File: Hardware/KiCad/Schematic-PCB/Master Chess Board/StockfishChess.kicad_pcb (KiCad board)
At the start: 4 copper layers, 100 x 120 mm, 72 parts, among them J1 ZF1-15-02-X-WT-X, J2 USB4110GFA, J4 ZF1-15-02-X-WT-X, U1 ESP32-S3-WROOM-2, U143 SN74AHCT125D, U144 USBLC6-2P6, U145 RUEF300, U146 RUEF300, U3 BQ24074RGT, U4 TPS61023DRLT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

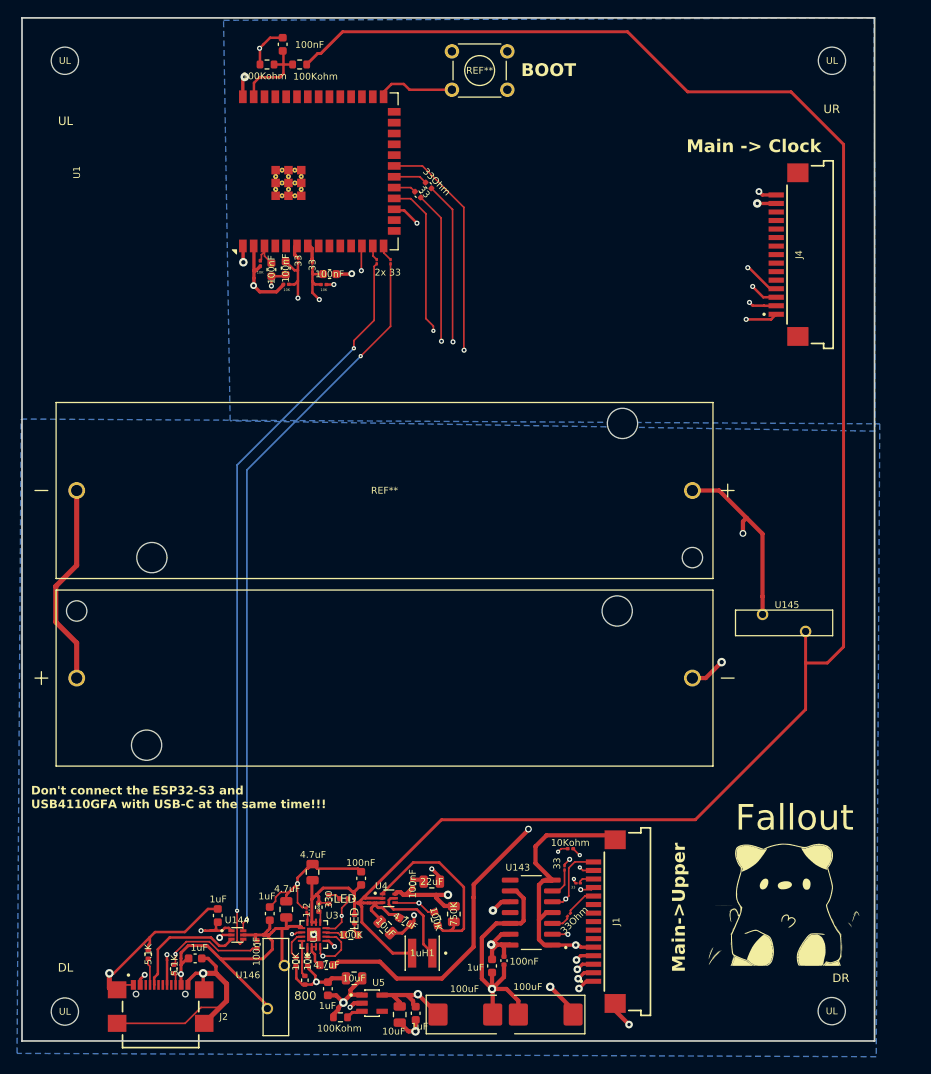
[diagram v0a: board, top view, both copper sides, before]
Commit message: Fixed some errors and finished BOM
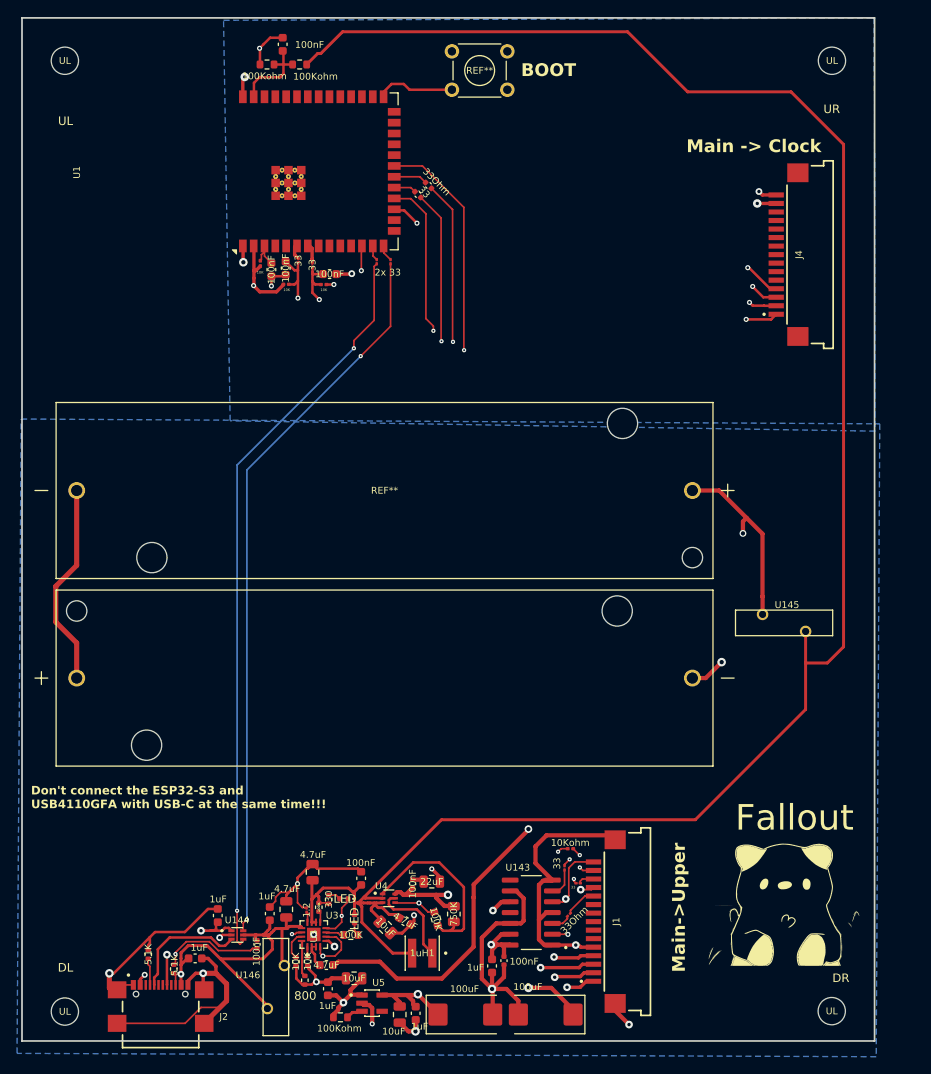
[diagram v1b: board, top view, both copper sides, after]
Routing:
- net +3.3V: track 206.1 -> 212.9 mm
- net +5V: track 41.0 -> 47.5 mm
- net GND: track 209.4 -> 211.1 mm

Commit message: Modified resistors
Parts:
- removed the 10Kohm at (139.1, 132.2)
- removed the 10Kohm at (110.1, 66.0)
- removed the 10Kohm at (105.7, 66.0)
- removed 2x 33: R_01005_0402Metric, Resistor_SMD:R_01005_0402Metric
- removed the 33Ohm at (138.4, 134.5)
- removed the 33Ohm at (108.8, 63.8)
- removed the 33Ohm at (140.0, 136.3)
- removed the 33Ohm at (138.9, 140.0)
- removed the 33Ohm at (107.1, 63.2)
- removed the REF** at (118.0, 63.4)
- added 10K: R_0402_1005Metric, Resistor_SMD:R_0402_1005Metric, F.Cu at (110.0, 66.2)
- added 10K: R_0402_1005Metric, Resistor_SMD:R_0402_1005Metric, F.Cu at (105.8, 66.3)
- added 10Kohm: R_0402_1005Metric, Resistor_SMD:R_0402_1005Metric, F.Cu at (139.0, 132.3)
- added 33: R_0402_1005Metric, Resistor_SMD:R_0402_1005Metric, F.Cu at (107.1, 63.6)
- added 33: R_0402_1005Metric, Resistor_SMD:R_0402_1005Metric, F.Cu at (118.2, 63.5)
- added 33: R_0402_1005Metric, Resistor_SMD:R_0402_1005Metric, F.Cu at (116.6, 63.6)
- added 33: R_0402_1005Metric, Resistor_SMD:R_0402_1005Metric, F.Cu at (137.8, 134.0)
- added 33: R_0402_1005Metric, Resistor_SMD:R_0402_1005Metric, F.Cu at (108.7, 63.6)
- added 33: R_0402_1005Metric, Resistor_SMD:R_0402_1005Metric, F.Cu at (139.2, 139.9)
- added 33: R_0402_1005Metric, Resistor_SMD:R_0402_1005Metric, F.Cu at (139.7, 135.8)
- 1.2: value R_01005_0402Metric -> R_0402_1005Metric; footprint Resistor_SMD:R_01005_0402Metric -> Resistor_SMD:R_0402_1005Metric
- moved 1.2 0.71 mm to (107.6, 138.9), turned to -90 degrees
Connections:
- 1.2 pad 1: Net-(U3-ILIM) -> GND
- 1.2 pad 2: GND -> Net-(U3-ILIM)
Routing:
- net GND: track 211.1 -> 209.9 mm
- net Net-(U1-IO13): track 100.4 -> 101.0 mm
- net /CLK 5V: track 10.2 -> 10.8 mm
- net Net-(J4-Pad01): track 64.6 -> 64.1 mm
- net +3.3V: track 212.9 -> 212.4 mm

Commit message: Added pulups to hall effect
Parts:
- removed the 1uF at (97.7, 140.1)
- added 100: C_0402_1005Metric, Capacitor_SMD:C_0402_1005Metric, F.Cu at (101.0, 65.1)
- added 22uF: C_1206_3216Metric, Capacitor_SMD:C_1206_3216Metric, F.Cu at (101.0, 69.1)
- added 3.3K: R_0402_1005Metric, Resistor_SMD:R_0402_1005Metric, F.Cu at (126.0, 55.2)
- added 6.8K: R_0402_1005Metric, Resistor_SMD:R_0402_1005Metric, F.Cu at (122.0, 50.5)
- turned REF** to 0 degrees
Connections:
- 4.7uF pad 1: VBUS -> BAT
- 4.7uF pad 2: VBUS -> BAT
- REF** pad N: Net-(BT1-PadN) -> GND
- REF** pad P: VBUS -> BAT
- REF** pad P: Net-(BT1-PadN) -> BAT
- U145 pad P$1: VBUS -> BAT
- U3 pad 2: VBUS -> BAT
- U3 pad 3: VBUS -> BAT
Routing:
- net BAT: track 0.00 -> 121.5 mm, vias 0 -> 2
- net VBUS: track 399.3 -> 293.9 mm, vias 4 -> 2
- net GND: track 209.9 -> 238.3 mm
- net Net-(BT1-PadN): track 24.0 -> 0.00 mm
- net +3.3V: track 212.4 -> 217.9 mm
- net +5V: track 47.5 -> 51.1 mm, vias 7 -> 6
- net Net-(U1-IO13): track 101.0 -> 102.1 mm
- net Net-(J2-DP2): track 13.9 -> 13.1 mm

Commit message: Had an excess voltage divider
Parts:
- removed 3.3K, 6.8K: R_0402_1005Metric, Resistor_SMD:R_0402_1005Metric
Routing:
- net GND: track 238.3 -> 237.1 mm, vias 25 -> 24
